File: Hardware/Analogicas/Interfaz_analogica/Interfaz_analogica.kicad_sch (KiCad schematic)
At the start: 1 part, among them U1 LM741

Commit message: Interfaz analógica
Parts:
- added C1, C2, C3, C4: 10nF, symbol Device:C
- added J0: Screw_Terminal_01x07, symbol Connector:Screw_Terminal_01x07
- added J1-1, J1-2, J2-1, J2-2, J3-1, J3-2, J4-1, J4-2, J5-1, J5-2, J6-1, J6-2, J7-1, J7-2, J8-1, J8-2: Screw_Terminal_01x01, symbol Connector:Screw_Terminal_01x01
- added J9: Screw_Terminal_01x06, symbol Connector:Screw_Terminal_01x06
- added Q1, Q2, Q3, Q4: 2N2222, Package_TO_SOT_THT:TO-39-3, symbol Transistor_BJT:2N2219
- added U2, U3, U4: LM741, symbol Amplifier_Operational:LM741
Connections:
- net at U1.2 (-): now also U1.6, J1-1.1 (Pin_1)
- net at U1.3 (+): now also C1.1, J0.4 (Pin_4)
- net at U1.4 (V-): now also J0.2 (Pin_2), U2.4 (V-), U3.4 (V-), U4.4 (V-)
- net at U1.7 (V+): now also J0.1 (Pin_1), U2.7 (V+), U3.7 (V+), U4.7 (V+)
- new net: J6-2.1 (Pin_1), J9.4 (Pin_4), Q2.1 (E)
- new net: J7-2.1 (Pin_1), J9.5 (Pin_5), Q3.1 (E)
- new net: C3.1, J0.6 (Pin_6), U3.3 (+)
- new net: J3-1.1 (Pin_1), U3.2 (-), U3.6
- new net: J4-1.1 (Pin_1), U4.2 (-), U4.6
- new net: C4.1, J0.7 (Pin_7), U4.3 (+)
- new net: J2-1.1 (Pin_1), U2.2 (-), U2.6
- new net: C2.1, J0.5 (Pin_5), U2.3 (+)
- new net: J2-2.1 (Pin_1), Q2.2 (B)
- new net: J9.1 (Pin_1), Q1.3 (C), Q2.3 (C), Q3.3 (C), Q4.3 (C)
- new net: J5-2.1 (Pin_1), J9.3 (Pin_3), Q1.1 (E)
- new net: J8-2.1 (Pin_1), J9.6 (Pin_6), Q4.1 (E)
- new net: J4-2.1 (Pin_1), Q4.2 (B)
- new net: J3-2.1 (Pin_1), Q3.2 (B)
- new net: J1-2.1 (Pin_1), Q1.2 (B)
- new net GNDREF: C1.2, C2.2, C3.2, C4.2, J0.3 (Pin_3), J5-1.1 (Pin_1), J6-1.1 (Pin_1), J7-1.1 (Pin_1), J8-1.1 (Pin_1), J9.2 (Pin_2)
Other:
- moved on the sheet: U1

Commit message: Referencias a los componentes de los circuitos
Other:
- note added: "Interfaz de señales analógicas"
- note added: "Los conectores a la salida de los amplificadores operacionales son para colocar resistencias que limitarán la corriente de base (Ib) de cada transistor Los conectores que están entre los emisores y GND son para colocar resistencias que limitarán la corriente de colector (Ic) de cada transistor Estas resistencias, según el datasheet del transistor 2n2222 se eligen con base en: Ic = 150 mA, Ib = 15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"
- company: (none) -> Digicontrol
- title: (none) -> Interfaz analógica
- moved on the sheet: C1, C2, C3, C4, J0, J1-1, J1-2, J2-1, J2-2, J3-1, J3-2, J4-1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

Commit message: Footprint para el LM741
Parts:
- U1, U2, U3, U4: footprint (none) -> LM741_TH:LM471_TH
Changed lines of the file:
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@@
 			)
 		)
-		(property "Footprint" ""
+		(property "Footprint" "LM741_TH:LM471_TH"
 			(at 142.24 120.65 0)
 			(effects
@@
 			)
 		)
-		(property "Footprint" ""
+		(property "Footprint" "LM741_TH:LM471_TH"
 			(at 142.24 69.85 0)
 			(effects
@@
 			)
 		)
-		(property "Footprint" ""
+		(property "Footprint" "LM741_TH:LM471_TH"
 			(at 142.24 95.25 0)
 			(effects
@@
 			)
 		)
-		(property "Footprint" ""
+		(property "Footprint" "LM741_TH:LM471_TH"
 			(at 142.24 44.45 0)
 			(effects

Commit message: Primera versión de la PCB para la interfaz analógica
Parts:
- C1, C2, C3, C4: footprint (none) -> Capacitor_THT:C_Disc_D4.3mm_W1.9mm_P5.00mm
- J0: footprint (none) -> TerminalBlock_Phoenix:TerminalBlock_Phoenix_PT-1,5-7-3.5-H_1x07_P3.50mm_Horizontal
- J1-1, J1-2, J2-1, J2-2, J3-1, J3-2, J4-1, J4-2, J5-1, J5-2, J6-1, J6-2, J7-1, J7-2, J8-1, J8-2: footprint (none) -> TerminalBlock_MetzConnect:TerminalBlock_MetzConnect_360271_1x01_Horizontal_ScrewM3.0_Boxed
- J9: footprint (none) -> TerminalBlock_Phoenix:TerminalBlock_Phoenix_PT-1,5-6-3.5-H_1x06_P3.50mm_Horizontal
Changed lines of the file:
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@@
 			)
 		)
-		(property "Footprint" ""
+		(property "Footprint" "TerminalBlock_MetzConnect:TerminalBlock_MetzConnect_360271_1x01_Horizontal_ScrewM3.0_Boxed"
 			(at 204.47 83.82 0)
 			(effects
@@
 			)
 		)
-		(property "Footprint" ""
+		(property "Footprint" "TerminalBlock_MetzConnect:TerminalBlock_MetzConnect_360271_1x01_Horizontal_ScrewM3.0_Boxed"
 			(at 204.47 109.22 0)
 			(effects
@@
 			)
 		)
-		(property "Footprint" ""
+		(property "Footprint" "Capacitor_THT:C_Disc_D4.3mm_W1.9mm_P5.00mm"
 			(at 77.1652 115.57 0)
 			(effects
@@
 			)
 		)
-		(property "Footprint" ""
+		(property "Footprint" "TerminalBlock_MetzConnect:TerminalBlock_MetzConnect_360271_1x01_Horizontal_ScrewM3.0_Boxed"
 			(at 168.91 96.52 0)
 			(effects
@@
 			)
 		)
-		(property "Footprint" ""
+		(property "Footprint" "TerminalBlock_MetzConnect:TerminalBlock_MetzConnect_360271_1x01_Horizontal_ScrewM3.0_Boxed"
 			(at 196.85 109.22 0)
 			(effects
@@
 			)
 		)
-		(property "Footprint" ""
+		(property "Footprint" "TerminalBlock_MetzConnect:TerminalBlock_MetzConnect_360271_1x01_Horizontal_ScrewM3.0_Boxed"
 			(at 196.85 83.82 0)
 			(effects
@@
 			)
 		)
-		(property "Footprint" ""
+		(property "Footprint" "TerminalBlock_MetzConnect:TerminalBlock_MetzConnect_360271_1x01_Horizontal_ScrewM3.0_Boxed"
 			(at 196.85 134.62 0)
 			(effects
@@
 			)
 		)
-		(property "Footprint" ""
+		(property "Footprint" "TerminalBlock_Phoenix:TerminalBlock_Phoenix_PT-1,5-7-3.5-H_1x07_P3.50mm_Horizontal"
 			(at 43.18 66.04 0)
 			(effects
@@
 			)
 		)
-		(property "Footprint" ""
+		(property "Footprint" "TerminalBlock_MetzConnect:TerminalBlock_MetzConnect_360271_1x01_Horizontal_ScrewM3.0_Boxed"
 			(at 168.91 71.12 0)
 			(effects
@@
 			)
 		)
-		(property "Footprint" ""
+		(property "Footprint" "TerminalBlock_Phoenix:TerminalBlock_Phoenix_PT-1,5-6-3.5-H_1x06_P3.50mm_Horizontal"
 			(at 245.11 86.36 0)
 			(effects
@@
 			)
 		)
-		(property "Footprint" ""
+		(property "Footprint" "TerminalBlock_MetzConnect:TerminalBlock_MetzConnect_360271_1x01_Horizontal_ScrewM3.0_Boxed"
 			(at 168.91 121.92 0)
 			(effects
@@
 			)
 		)
-		(property "Footprint" ""
+		(property "Footprint" "TerminalBlock_MetzConnect:TerminalBlock_MetzConnect_360271_1x01_Horizontal_ScrewM3.0_Boxed"
 			(at 204.47 58.42 0)
 			(effects
@@
 			)
 		)
-		(property "Footprint" ""
+		(property "Footprint" "TerminalBlock_MetzConnect:TerminalBlock_MetzConnect_360271_1x01_Horizontal_ScrewM3.0_Boxed"
 			(at 179.07 96.52 0)
 			(effects
@@
 			)
 		)
-		(property "Footprint" ""
+		(property "Footprint" "TerminalBlock_MetzConnect:TerminalBlock_MetzConnect_360271_1x01_Horizontal_ScrewM3.0_Boxed"
 			(at 179.07 121.92 0)
 			(effects
@@
 			)
 		)
-		(property "Footprint" ""
+		(property "Footprint" "TerminalBlock_MetzConnect:TerminalBlock_MetzConnect_360271_1x01_Horizontal_ScrewM3.0_Boxed"
 			(at 204.47 134.62 0)
 			(effects
@@
 			)
 		)
-		(property "Footprint" ""
+		(property "Footprint" "TerminalBlock_MetzConnect:TerminalBlock_MetzConnect_360271_1x01_Horizontal_ScrewM3.0_Boxed"
 			(at 179.07 45.72 0)
 			(effects
@@
 			)
 		)
-		(property "Footprint" ""
+		(property "Footprint" "TerminalBlock_MetzConnect:TerminalBlock_MetzConnect_360271_1x01_Horizontal_ScrewM3.0_Boxed"
 			(at 196.85 58.42 0)
 			(effects
@@
 			)
 		)
-		(property "Footprint" ""
+		(property "Footprint" "Capacitor_THT:C_Disc_D4.3mm_W1.9mm_P5.00mm"
 			(at 72.0852 128.27 0)
 			(effects
@@
 			)
 		)
-		(property "Footprint" ""
+		(property "Footprint" "Capacitor_THT:C_Disc_D4.3mm_W1.9mm_P5.00mm"
 			(at 88.5952 90.17 0)
 			(effects
@@
 			)
 		)
-		(property "Footprint" ""
+		(property "Footprint" "Capacitor_THT:C_Disc_D4.3mm_W1.9mm_P5.00mm"
 			(at 82.2452 102.87 0)
 			(effects
@@
 			)
 		)
-		(property "Footprint" ""
+		(property "Footprint" "TerminalBlock_MetzConnect:TerminalBlock_MetzConnect_360271_1x01_Horizontal_ScrewM3.0_Boxed"
 			(at 179.07 71.12 0)
 			(effects
@@
 			)
 		)
-		(property "Footprint" ""
+		(property "Footprint" "TerminalBlock_MetzConnect:TerminalBlock_MetzConnect_360271_1x01_Horizontal_ScrewM3.0_Boxed"
 			(at 168.91 45.72 0)
 			(effects

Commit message: Actualización del codigo del ESP32
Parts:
- U1, U2, U3, U4: footprint LM741_TH:LM471_TH -> LM741_TH:LM741_TH
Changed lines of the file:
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@@
 			)
 		)
-		(property "Footprint" "LM741_TH:LM471_TH"
+		(property "Footprint" "LM741_TH:LM741_TH"
 			(at 142.24 120.65 0)
 			(effects
@@
 			)
 		)
-		(property "Footprint" "LM741_TH:LM471_TH"
+		(property "Footprint" "LM741_TH:LM741_TH"
 			(at 142.24 69.85 0)
 			(effects
@@
 			)
 		)
-		(property "Footprint" "LM741_TH:LM471_TH"
+		(property "Footprint" "LM741_TH:LM741_TH"
 			(at 142.24 95.25 0)
 			(effects
@@
 			)
 		)
-		(property "Footprint" "LM741_TH:LM471_TH"
+		(property "Footprint" "LM741_TH:LM741_TH"
 			(at 142.24 44.45 0)
 			(effects

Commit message: Creación de PCB's con los archivos gerber y drill
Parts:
- removed J0: Screw_Terminal_01x07, TerminalBlock_Phoenix:TerminalBlock_Phoenix_PT-1,5-7-3.5-H_1x07_P3.50mm_Horizontal, symbol Connector:Screw_Terminal_01x07
- removed J9: Screw_Terminal_01x06, TerminalBlock_Phoenix:TerminalBlock_Phoenix_PT-1,5-6-3.5-H_1x06_P3.50mm_Horizontal, symbol Connector:Screw_Terminal_01x06
- added J0_1, J0_2, J0_3, J9_1, J9_2: Screw_Terminal_01x03, TerminalBlock_Phoenix:TerminalBlock_Phoenix_PT-1,5-3-3.5-H_1x03_P3.50mm_Horizontal, symbol Connector:Screw_Terminal_01x03
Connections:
- net GNDREF: now also J0_1.3 (Pin_3), J9_1.2 (Pin_2)
- net at J6-2.1 (Pin_1), Q2.1 (E): now also J9_2.3 (Pin_3)
- net at J7-2.1 (Pin_1), Q3.1 (E): now also J9_2.2 (Pin_2)
- net at C3.1, U3.3 (+): now also J0_2.3 (Pin_3)
- net at C4.1, U4.3 (+): now also J0_3.1 (Pin_1)
- net at U1.4 (V-), U2.4 (V-), U3.4 (V-)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: now also J0_1.2 (Pin_2)
- net at U1.7 (V+), U2.7 (V+), U3.7 (V+)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: now also J0_1.1 (Pin_1)
- net at C2.1, U2.3 (+): now also J0_2.2 (Pin_2)
- net at Q1.3 (C), Q2.3 (C), Q3.3 (C)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: now also J9_1.3 (Pin_3)
- net at C1.1, U1.3 (+): now also J0_2.1 (Pin_1)
- net at J5-2.1 (Pin_1), Q1.1 (E): now also J9_1.1 (Pin_1)
- net at J8-2.1 (Pin_1), Q4.1 (E): now also J9_2.1 (Pin_1)
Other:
- note added: "Los conectores a la salida de los amplificadores operacionales son para colocar resistencias que limitarán la corriente de base (Ib) de cada transistor, con base en simulaciones, se sugiere resistencia de 7.5 Kilo ohmios para señales que oscilen entre 0-10 voltios y 1.2 Kilo ohmios para señales que oscilen entre 0-5 voltios Los conectores que están entre los emisores y GND son para colocar resist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"
- note removed: "Los conectores a la salida de los amplificadores operacionales son para colocar resistencias que limitarán la corriente de base (Ib) de cada transistor Los conectores que están entre los emisores y GND son para colocar resistencias que limitarán la corriente de colector (Ic) de cada transistor Estas resistencias, según el datasheet del transistor 2n2222 se eligen con base en: Ic = 150 mA, Ib = 15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"
- moved on the sheet: J1-1, J1-2, J2-1, J2-2, J3-1, J3-2, J4-1, J4-2, J5-1, J5-2, J6-1, J6-2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

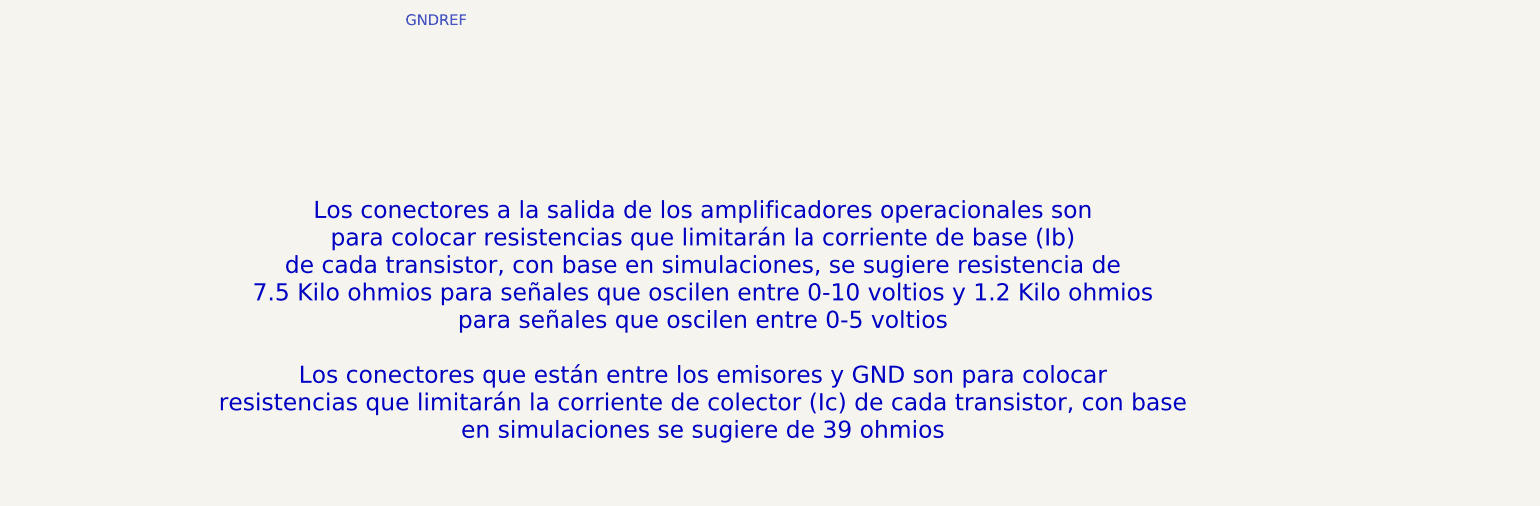
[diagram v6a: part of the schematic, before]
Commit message: Esquematicos de las PCB
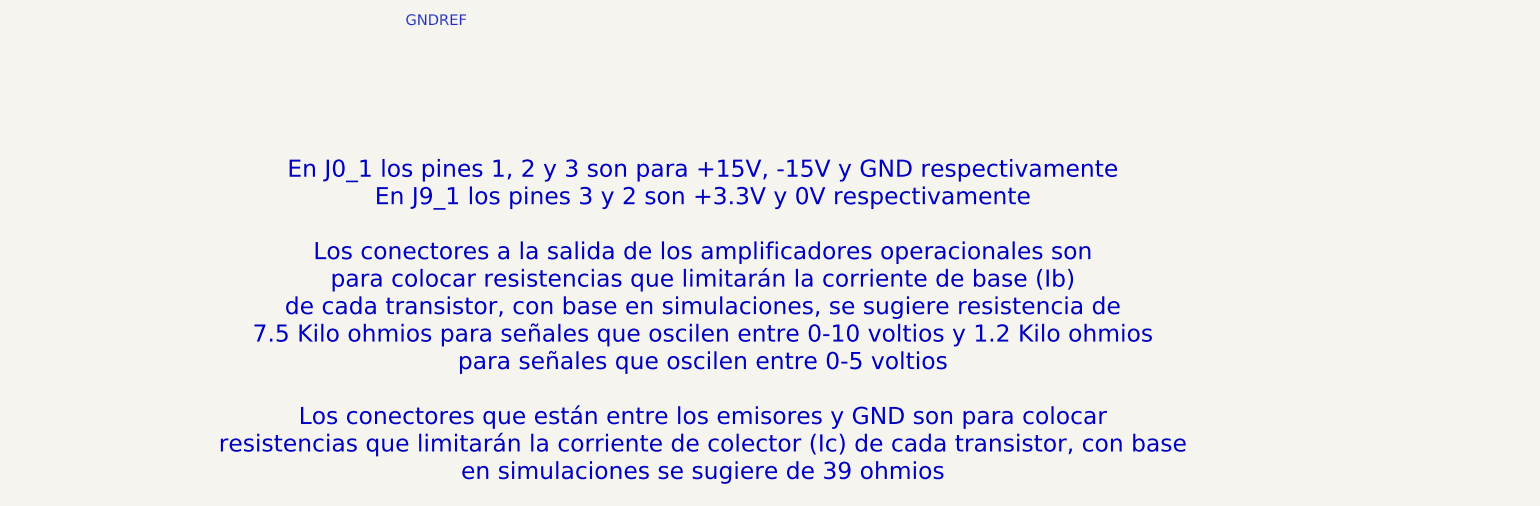
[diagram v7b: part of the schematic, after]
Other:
- note added: "En J0_1 los pines 1, 2 y 3 son para +15V, -15V y GND respectivamente En J9_1 los pines 3 y 2 son +3.3V y 0V respectivamente Los conectores a la salida de los amplificadores operacionales son para colocar resistencias que limitarán la corriente de base (Ib) de cada transistor, con base en simulaciones, se sugiere resistencia de 7.5 Kilo ohmios para señales que oscilen entre 0-10 voltios y 1.2 Kilo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"
- note removed: "Los conectores a la salida de los amplificadores operacionales son para colocar resistencias que limitarán la corriente de base (Ib) de cada transistor, con base en simulaciones, se sugiere resistencia de 7.5 Kilo ohmios para señales que oscilen entre 0-10 voltios y 1.2 Kilo ohmios para señales que oscilen entre 0-5 voltios Los conectores que están entre los emisores y GND son para colocar resist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"
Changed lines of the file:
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@@
 		(company "Digicontrol")
 	)
-	(text "Los conectores a la salida de los amplificadores operacionales son \npara colocar resistencias que limitarán la corriente de base (Ib)\nde cada transistor, con base en simulaciones, se sugiere resistencia de\n7.5 Kilo ohmios para señales que oscilen entre 0-10 voltios y 1.2 Kilo ohmios\npara señales que oscilen entre 0-5 voltios\n\nLos conectores que están entre los emisores y GND son para colocar\nresistencias que limitarán la corriente de colector (Ic) de cada transistor, con base\nen simulaciones se sugiere de 39 ohmios\n\n"
+	(text "En J0_1 los pines 1, 2 y 3 son para +15V, -15V y GND respectivamente \nEn J9_1 los pines 3 y 2 son +3.3V y 0V respectivamente\n\nLos conectores a la salida de los amplificadores operacionales son \npara colocar resistencias que limitarán la corriente de base (Ib)\nde cada transistor, con base en simulaciones, se sugiere resistencia de\n7.5 Kilo ohmios para señales que oscilen entre 0-10 voltios y 1.2 Kilo ohmios\npara señales que oscilen entre 0-5 voltios\n\nLos conectores que están entre los emisores y GND son para colocar\nresistencias que limitarán la corriente de colector (Ic) de cada transistor, con base\nen simulaciones se sugiere de 39 ohmios\n\n"
 		(exclude_from_sim no)
 		(at 87.63 174.752 0)

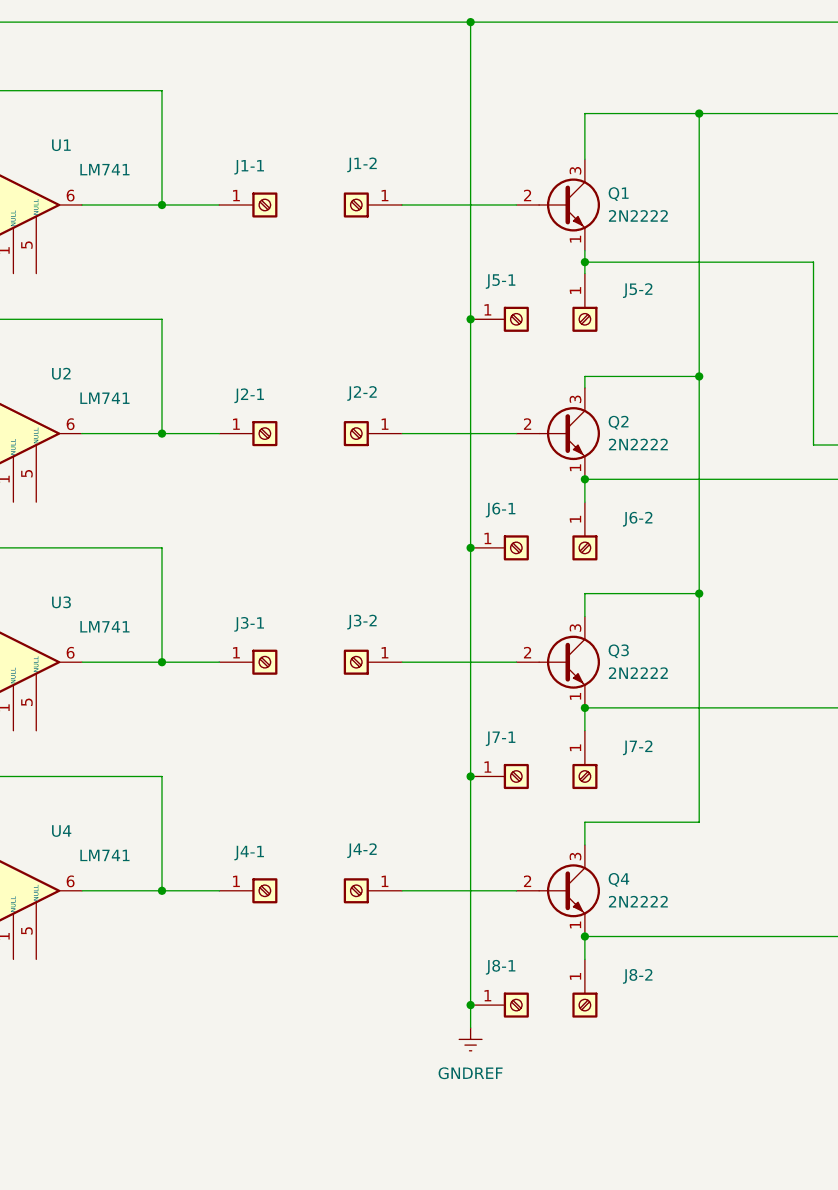
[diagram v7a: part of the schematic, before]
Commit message: Ajustes a las interfaces digital y analogica
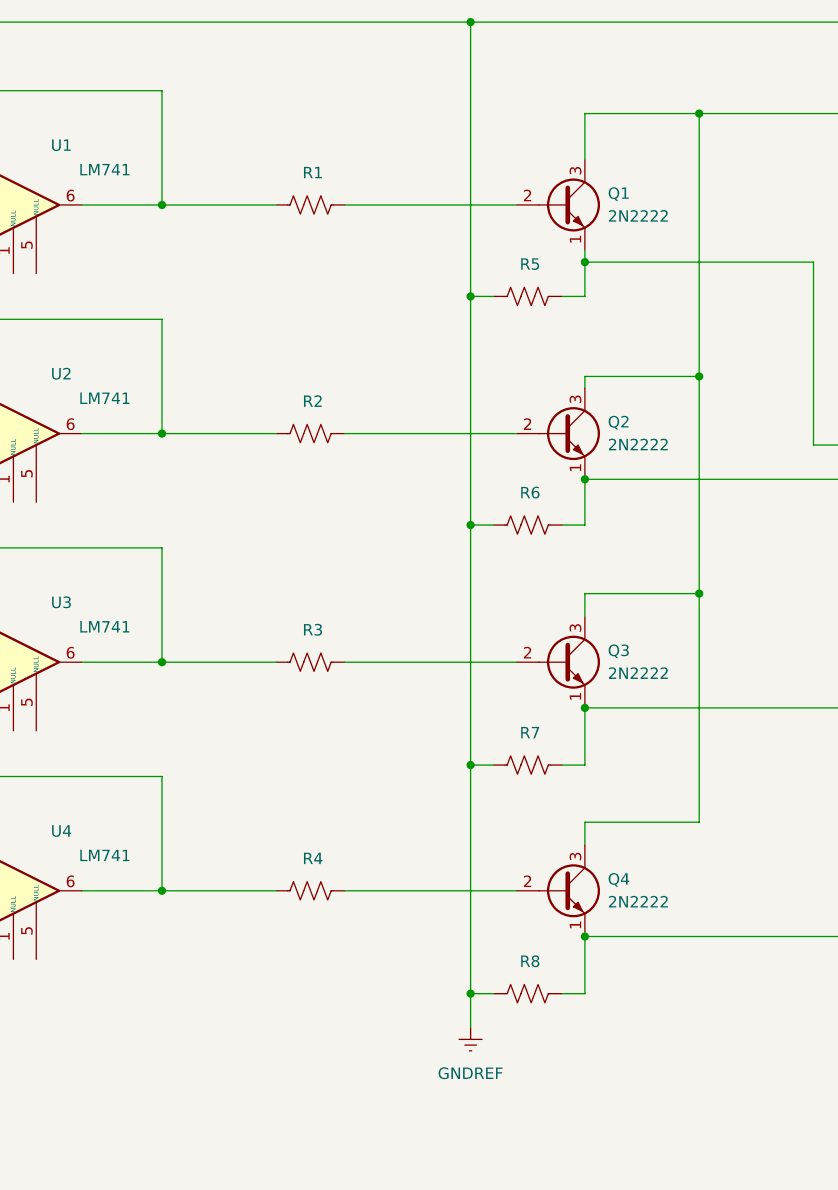
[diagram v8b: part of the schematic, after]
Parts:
- removed J1-1, J1-2, J2-1, J2-2, J3-1, J3-2, J4-1, J4-2, J5-1, J5-2, J6-1, J6-2, J7-1, J7-2, J8-1, J8-2: Screw_Terminal_01x01, TerminalBlock_MetzConnect:TerminalBlock_MetzConnect_360271_1x01_Horizontal_ScrewM3.0_Boxed, symbol Connector:Screw_Terminal_01x01
- added R1, R2, R3, R4, R5, R6, R7, R8: R_US, Resistor_THT:R_Axial_DIN0207_L6.3mm_D2.5mm_P7.62mm_Horizontal, symbol Device:R_US
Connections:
- net GNDREF: now also R5.1, R6.1, R7.1, R8.1
- net at J9_2.3 (Pin_3), Q2.1 (E): now also R6.2
- net at J9_2.2 (Pin_2), Q3.1 (E): now also R7.2
- net at U3.2 (-), U3.6: now also R3.1
- net at U4.2 (-), U4.6: now also R4.1
- net at U2.2 (-), U2.6: now also R2.1
- net at J9_1.1 (Pin_1), Q1.1 (E): now also R5.2
- net at Q2.2 (B): now also R2.2
- net at J9_2.1 (Pin_1), Q4.1 (E): now also R8.2
- net at Q4.2 (B): now also R4.2
- net at Q3.2 (B): now also R3.2
- net at Q1.2 (B): now also R1.2
- net at U1.2 (-), U1.6: now also R1.1
